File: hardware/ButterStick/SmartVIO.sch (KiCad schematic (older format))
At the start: 24 parts, among them J7 TagConnect, U19 ATmega328PB-MU, Y2 Resonator

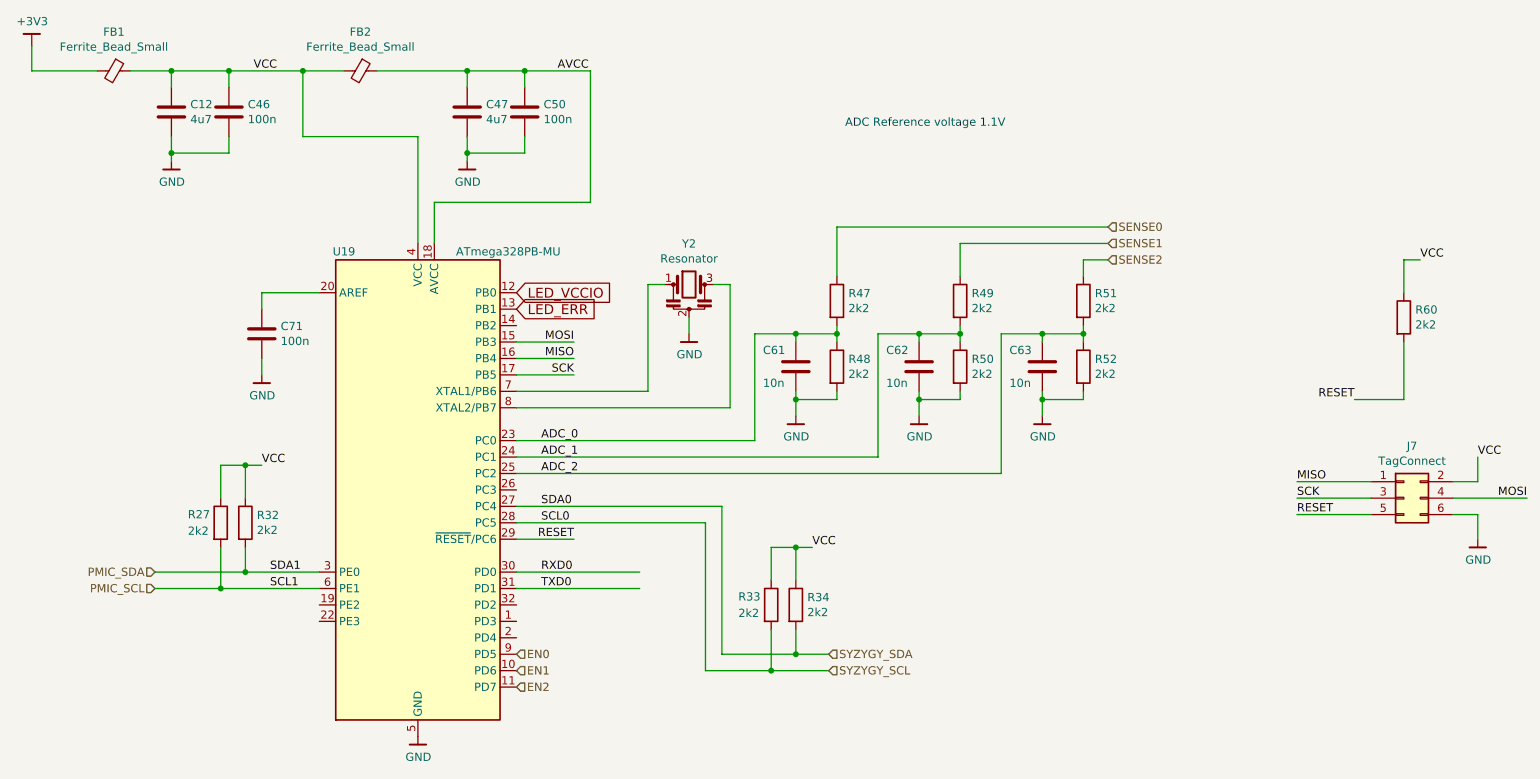
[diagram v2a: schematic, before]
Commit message: Finalised part values update BOM values to reflect. Swapped layers 4/5 due to stackup changes
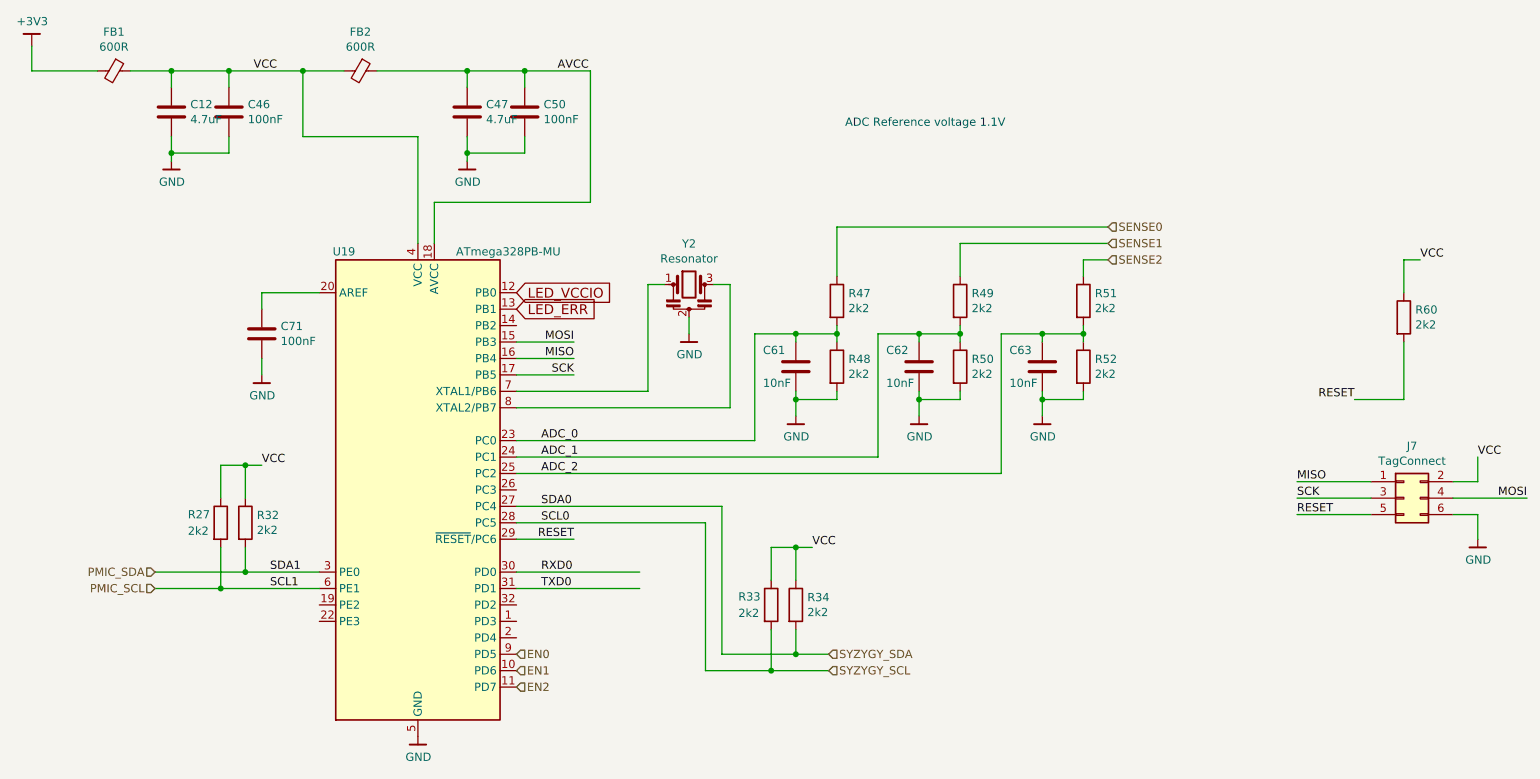
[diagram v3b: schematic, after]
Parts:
- C12, C47: value 4u7 -> 4.7uF; Mfg (none) -> Samsung Electro-Mechanics; PN (none) -> CL10A475KP8NNNC
- C46, C50, C71: value 100n -> 100nF; Mfg (none) -> Samsung Electro-Mechanics; PN (none) -> CL05B104KP5NNNC
- C61, C62, C63: value 10n -> 10nF; Mfg (none) -> Samsung Electro-Mechanics; PN (none) -> CL05B103KB5NNNC
- FB1, FB2: value Ferrite_Bead_Small -> 600R; Mfg (none) -> Samsung Electro-Mechanics; PN (none) -> CIM05U601NC
- R27, R32, R33, R34, R47, R48, R49, R50, R51, R52, R60: Mfg (none) -> Stackpole Electronics Inc; PN (none) -> RMCF0402FT2K20
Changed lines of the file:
@@
 EESchema Schematic File Version 4
 LIBS:ButterStick-cache
-EELAYER 26 0
+EELAYER 29 0
 EELAYER END
 $Descr A4 11693 8268
 encoding utf-8
-Sheet 13 13
-Title ""
-Date ""
-Rev ""
-Comp ""
+Sheet 4 13
+Title "ButterStick"
+Date "2019-03-19"
+Rev "r0_1"
+Comp "GsD"
 Comment1 ""
 Comment2 ""
@@
 P 1800 1400
 F 0 "FB1" V 1563 1400 50  0000 C CNN
-F 1 "Ferrite_Bead_Small" V 1654 1400 50  0000 C CNN
+F 1 "600R" V 1654 1400 50  0000 C CNN
 F 2 "pkl_dipol:L_0402" V 1730 1400 50  0001 C CNN
 F 3 "~" H 1800 1400 50  0001 C CNN
+F 4 "Samsung Electro-Mechanics" H 0   0   50  0001 C CNN "Mfg"
+F 5 "CIM05U601NC" H 0   0   50  0001 C CNN "PN"
 	1    1800 1400
 	0    1    1    0
@@
 P 3300 1400
 F 0 "FB2" V 3063 1400 50  0000 C CNN
-F 1 "Ferrite_Bead_Small" V 3154 1400 50  0000 C CNN
+F 1 "600R" V 3154 1400 50  0000 C CNN
 F 2 "pkl_dipol:L_0402" V 3230 1400 50  0001 C CNN
 F 3 "~" H 3300 1400 50  0001 C CNN
+F 4 "Samsung Electro-Mechanics" H 0   0   50  0001 C CNN "Mfg"
+F 5 "CIM05U601NC" H 0   0   50  0001 C CNN "PN"
 	1    3300 1400
 	0    1    1    0
@@
 Wire Wire Line
 	3050 4450 2600 4450
-Text Label 2750 4450 0    50   ~ 0
-SDA1
-Text Label 2750 4550 0    50   ~ 0
-SCL1
 Wire Wire Line
 	4250 4450 5000 4450
@@
 Text HLabel 6150 5050 2    50   Input ~ 0
 SYZYGY_SCL
-Text HLabel 2050 4450 0    50   Input ~ 0
-PMIC_SDA
-Text HLabel 2050 4550 0    50   Input ~ 0
-PMIC_SCL
 Text HLabel 7850 2350 2    50   Input ~ 0
 SENSE0
@@
 F 2 "pkl_dipol:R_0402" V 2530 4150 50  0001 C CNN
 F 3 "~" H 2600 4150 50  0001 C CNN
+F 4 "Stackpole Electronics Inc" H 0   0   50  0001 C CNN "Mfg"
+F 5 "RMCF0402FT2K20" H 0   0   50  0001 C CNN "PN"
 	1    2600 4150
 	1    0    0    -1
@@
 F 2 "pkl_dipol:R_0402" V 2380 4150 50  0001 C CNN
 F 3 "~" H 2450 4150 50  0001 C CNN
+F 4 "Stackpole Electronics Inc" H 0   0   50  0001 C CNN "Mfg"
+F 5 "RMCF0402FT2K20" H 0   0   50  0001 C CNN "PN"
 	1    2450 4150
 	1    0    0    -1
@@
 P 2150 1650
 F 0 "C12" H 2265 1696 50  0000 L CNN
-F 1 "4u7" H 2265 1605 50  0000 L CNN
+F 1 "4.7uF" H 2265 1605 50  0000 L CNN
 F 2 "pkl_dipol:C_0603" H 2188 1500 50  0001 C CNN
 F 3 "~" H 2150 1650 50  0001 C CNN
+F 4 "Samsung Electro-Mechanics" H 0   0   50  0001 C CNN "Mfg"
+F 5 "CL10A475KP8NNNC" H 0   0   50  0001 C CNN "PN"
 	1    2150 1650
 	1    0    0    -1
@@
 P 2500 1650
 F 0 "C46" H 2615 1696 50  0000 L CNN
-F 1 "100n" H 2615 1605 50  0000 L CNN
+F 1 "100nF" H 2615 1605 50  0000 L CNN
 F 2 "pkl_dipol:C_0402" H 2538 1500 50  0001 C CNN
 F 3 "~" H 2500 1650 50  0001 C CNN
+F 4 "Samsung Electro-Mechanics" H 0   0   50  0001 C CNN "Mfg"
+F 5 "CL05B104KP5NNNC" H 0   0   50  0001 C CNN "PN"
 	1    2500 1650
 	1    0    0    -1
@@
 P 3950 1650
 F 0 "C47" H 4065 1696 50  0000 L CNN
-F 1 "4u7" H 4065 1605 50  0000 L CNN
+F 1 "4.7uF" H 4065 1605 50  0000 L CNN
 F 2 "pkl_dipol:C_0603" H 3988 1500 50  0001 C CNN
 F 3 "~" H 3950 1650 50  0001 C CNN
+F 4 "Samsung Electro-Mechanics" H 0   0   50  0001 C CNN "Mfg"
+F 5 "CL10A475KP8NNNC" H 0   0   50  0001 C CNN "PN"
 	1    3950 1650
 	1    0    0    -1
@@
 P 4300 1650
 F 0 "C50" H 4415 1696 50  0000 L CNN
-F 1 "100n" H 4415 1605 50  0000 L CNN
+F 1 "100nF" H 4415 1605 50  0000 L CNN
 F 2 "pkl_dipol:C_0402" H 4338 1500 50  0001 C CNN
 F 3 "~" H 4300 1650 50  0001 C CNN
+F 4 "Samsung Electro-Mechanics" H 0   0   50  0001 C CNN "Mfg"
+F 5 "CL05B104KP5NNNC" H 0   0   50  0001 C CNN "PN"
 	1    4300 1650
 	1    0    0    -1
@@
 Connection ~ 2600 4450
 Wire Wire Line
-	2050 4550 2450 4550
-Wire Wire Line
-	2050 4450 2600 4450
-Wire Wire Line
 	2450 4300 2450 4550
 Connection ~ 2450 4550
@@
 F 2 "pkl_dipol:R_0402" V 5880 4650 50  0001 C CNN
 F 3 "~" H 5950 4650 50  0001 C CNN
+F 4 "Stackpole Electronics Inc" H 0   0   50  0001 C CNN "Mfg"
+F 5 "RMCF0402FT2K20" H 0   0   50  0001 C CNN "PN"
 	1    5950 4650
 	1    0    0    -1
@@
 F 2 "pkl_dipol:R_0402" V 5730 4650 50  0001 C CNN
 F 3 "~" H 5800 4650 50  0001 C CNN
+F 4 "Stackpole Electronics Inc" H 0   0   50  0001 C CNN "Mfg"
+F 5 "RMCF0402FT2K20" H 0   0   50  0001 C CNN "PN"
 	1    5800 4650
 	1    0    0    -1
@@
 F 2 "pkl_dipol:R_0402" V 7630 2800 50  0001 C CNN
 F 3 "~" H 7700 2800 50  0001 C CNN
+F 4 "Stackpole Electronics Inc" H 0   0   50  0001 C CNN "Mfg"
+F 5 "RMCF0402FT2K20" H 0   0   50  0001 C CNN "PN"
 	1    7700 2800
 	1    0    0    -1
@@
 F 2 "pkl_dipol:R_0402" V 7630 3200 50  0001 C CNN
 F 3 "~" H 7700 3200 50  0001 C CNN
+F 4 "Stackpole Electronics Inc" H 0   0   50  0001 C CNN "Mfg"
+F 5 "RMCF0402FT2K20" H 0   0   50  0001 C CNN "PN"
 	1    7700 3200
 	1    0    0    -1
@@
 P 7450 3200
 F 0 "C63" H 7250 3300 50  0000 L CNN
-F 1 "10n" H 7250 3100 50  0000 L CNN
+F 1 "10nF" H 7250 3100 50  0000 L CNN
 F 2 "pkl_dipol:C_0402" H 7488 3050 50  0001 C CNN
 F 3 "~" H 7450 3200 50  0001 C CNN
+F 4 "Samsung Electro-Mechanics" H 0   0   50  0001 C CNN "Mfg"
+F 5 "CL05B103KB5NNNC" H 0   0   50  0001 C CNN "PN"
 	1    7450 3200
 	1    0    0    -1
@@
 F 2 "pkl_dipol:R_0402" V 6880 2800 50  0001 C CNN
 F 3 "~" H 6950 2800 50  0001 C CNN
+F 4 "Stackpole Electronics Inc" H 0   0   50  0001 C CNN "Mfg"
+F 5 "RMCF0402FT2K20" H 0   0   50  0001 C CNN "PN"
 	1    6950 2800
 	1    0    0    -1
@@
 F 2 "pkl_dipol:R_0402" V 6880 3200 50  0001 C CNN
 F 3 "~" H 6950 3200 50  0001 C CNN
+F 4 "Stackpole Electronics Inc" H 0   0   50  0001 C CNN "Mfg"
+F 5 "RMCF0402FT2K20" H 0   0   50  0001 C CNN "PN"
 	1    6950 3200
 	1    0    0    -1
@@
 P 6700 3200
 F 0 "C62" H 6500 3300 50  0000 L CNN
-F 1 "10n" H 6500 3100 50  0000 L CNN
+F 1 "10nF" H 6500 3100 50  0000 L CNN
 F 2 "pkl_dipol:C_0402" H 6738 3050 50  0001 C CNN
 F 3 "~" H 6700 3200 50  0001 C CNN
+F 4 "Samsung Electro-Mechanics" H 0   0   50  0001 C CNN "Mfg"
+F 5 "CL05B103KB5NNNC" H 0   0   50  0001 C CNN "PN"
 	1    6700 3200
 	1    0    0    -1
@@
 F 2 "pkl_dipol:R_0402" V 6130 2800 50  0001 C CNN
 F 3 "~" H 6200 2800 50  0001 C CNN
+F 4 "Stackpole Electronics Inc" H 0   0   50  0001 C CNN "Mfg"
+F 5 "RMCF0402FT2K20" H 0   0   50  0001 C CNN "PN"
 	1    6200 2800
 	1    0    0    -1
@@
 F 2 "pkl_dipol:R_0402" V 6130 3200 50  0001 C CNN
 F 3 "~" H 6200 3200 50  0001 C CNN
+F 4 "Stackpole Electronics Inc" H 0   0   50  0001 C CNN "Mfg"
+F 5 "RMCF0402FT2K20" H 0   0   50  0001 C CNN "PN"
 	1    6200 3200
 	1    0    0    -1
@@
 P 5950 3200
 F 0 "C61" H 5750 3300 50  0000 L CNN
-F 1 "10n" H 5750 3100 50  0000 L CNN
+F 1 "10nF" H 5750 3100 50  0000 L CNN
 F 2 "pkl_dipol:C_0402" H 5988 3050 50  0001 C CNN
 F 3 "~" H 5950 3200 50  0001 C CNN
+F 4 "Samsung Electro-Mechanics" H 0   0   50  0001 C CNN "Mfg"
+F 5 "CL05B103KB5NNNC" H 0   0   50  0001 C CNN "PN"
 	1    5950 3200
 	1    0    0    -1
@@
 P 2700 3000
 F 0 "C71" H 2815 3046 50  0000 L CNN
-F 1 "100n" H 2815 2955 50  0000 L CNN
+F 1 "100nF" H 2815 2955 50  0000 L CNN
 F 2 "pkl_dipol:C_0402" H 2738 2850 50  0001 C CNN
 F 3 "~" H 2700 3000 50  0001 C CNN
+F 4 "Samsung Electro-Mechanics" H 0   0   50  0001 C CNN "Mfg"
+F 5 "CL05B104KP5NNNC" H 0   0   50  0001 C CNN "PN"
 	1    2700 3000
 	1    0    0    -1
@@
 F 2 "pkl_dipol:R_0402" V 9580 2900 50  0001 C CNN
 F 3 "~" H 9650 2900 50  0001 C CNN
+F 4 "Stackpole Electronics Inc" H 0   0   50  0001 C CNN "Mfg"
+F 5 "RMCF0402FT2K20" H 0   0   50  0001 C CNN "PN"
 	1    9650 2900
 	1    0    0    -1
@@
 Wire Wire Line
 	9650 2550 9750 2550
+Wire Wire Line
+	2050 4450 2600 4450
+Wire Wire Line
+	2050 4550 2450 4550
+Text HLabel 2050 4550 0    50   Input ~ 0
+PMIC_SCL
+Text HLabel 2050 4450 0    50   Input ~ 0
+PMIC_SDA
+Text Label 2750 4550 0    50   ~ 0
+SCL1
+Text Label 2750 4450 0    50   ~ 0
+SDA1
 $EndSCHEMATC
